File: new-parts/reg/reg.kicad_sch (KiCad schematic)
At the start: 51 parts, among them J1 BHR-10-VUA, J2 BHR-10-VUA, J3 BHR-10-VUA, J4 BHR-10-VUA, J5 Conn_01x01, J6 Conn_02x02_Odd_Even, K1 J104D2C12VDC.15S, K10 J104D2C12VDC.15S, K11 J104D2C12VDC.15S, K12 J104D2C12VDC.15S, K2 J104D2C12VDC.15S, K3 J104D2C12VDC.15S, K4 J104D2C12VDC.15S, K5 J104D2C12VDC.15S, K6 J104D2C12VDC.15S, K7 J104D2C12VDC.15S, K8 J104D2C12VDC.15S, K9 J104D2C12VDC.15S

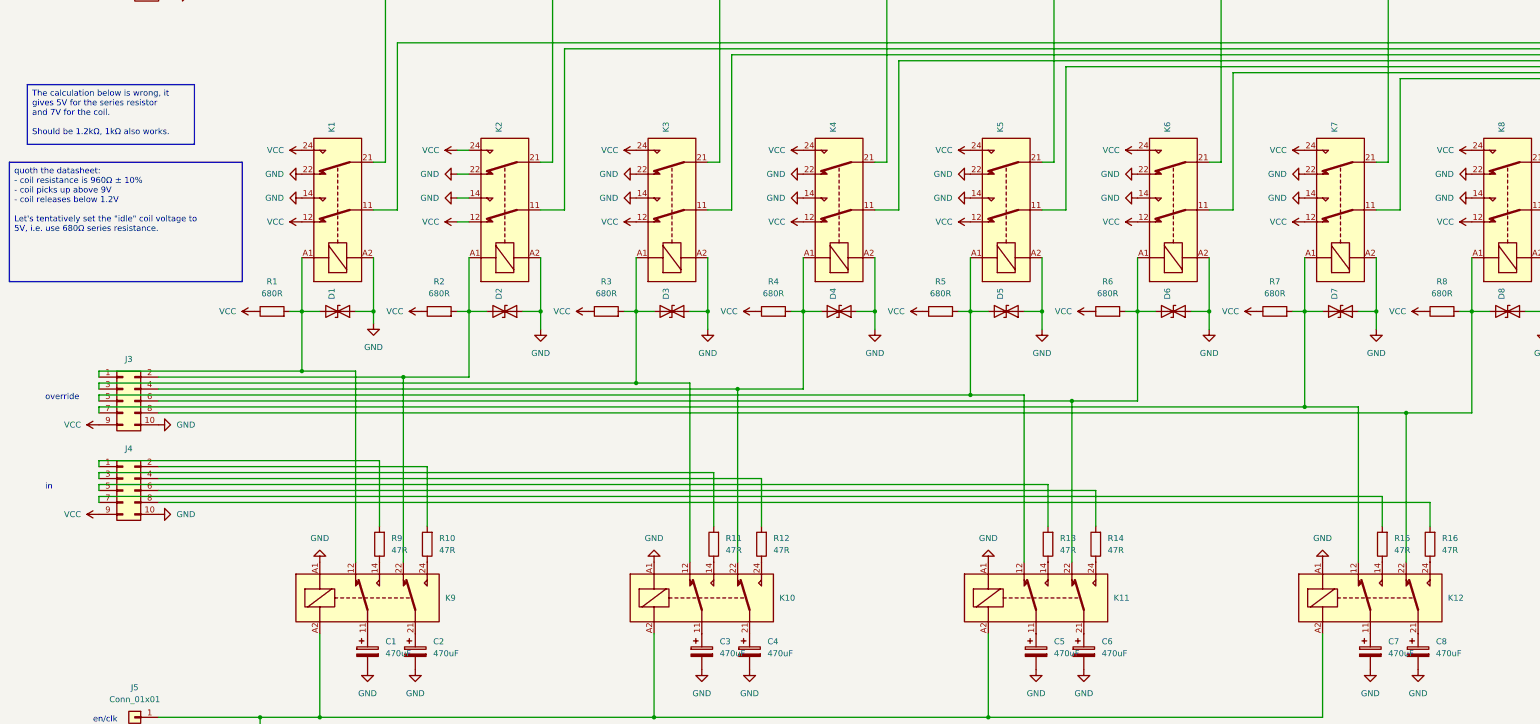
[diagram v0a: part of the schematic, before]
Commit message: reg: Correct "latching" coils' voltage dividers (finally).
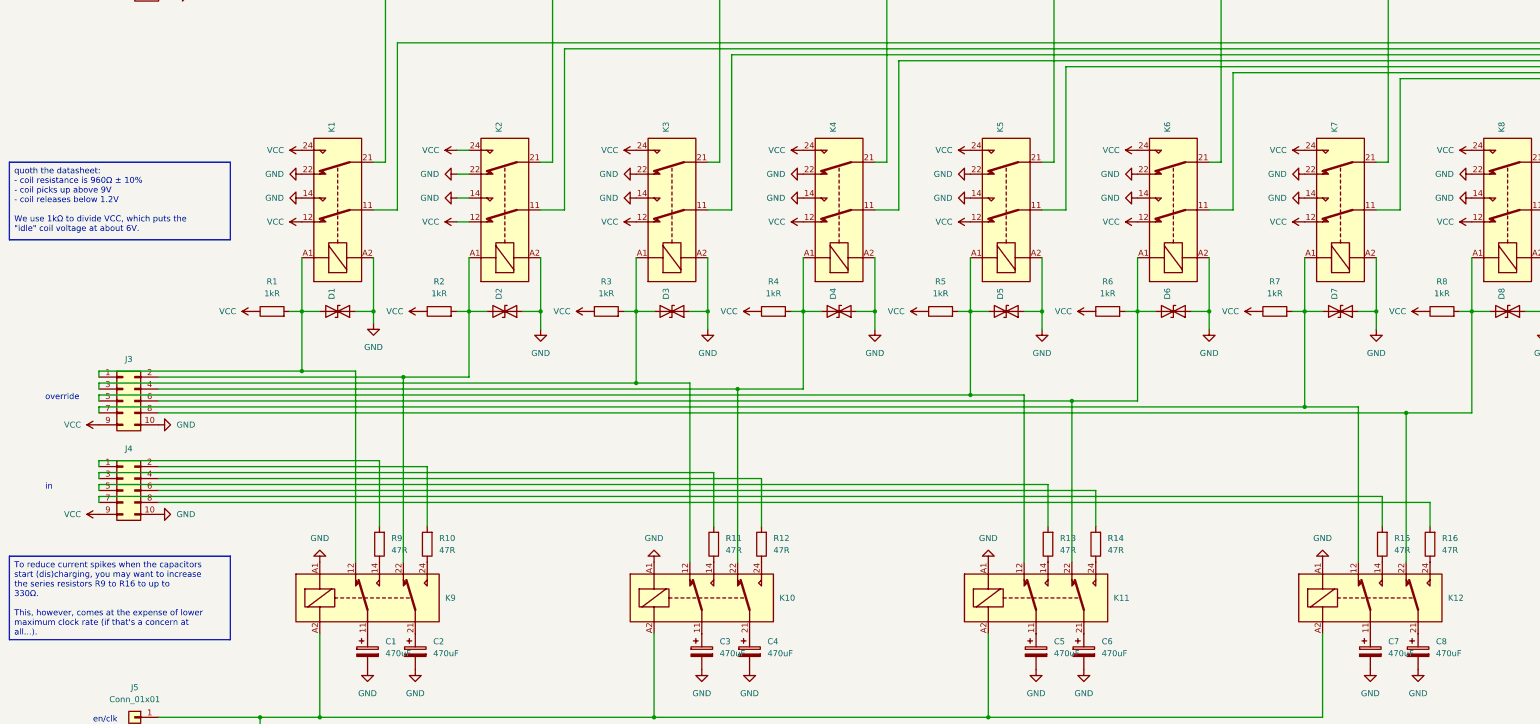
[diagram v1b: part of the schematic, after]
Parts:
- R1, R2, R3, R4, R5, R6, R7, R8: value 680R -> 1kR
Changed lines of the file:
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@@
 		)
 	)
-	(text_box "quoth the datasheet:\n- coil resistance is 960Ω ± 10%\n- coil picks up above 9V\n- coil releases below 1.2V\n\nLet's tentatively set the \"idle\" coil voltage to 5V, i.e. use 680Ω series resistance."
+	(text_box "quoth the datasheet:\n- coil resistance is 960Ω ± 10%\n- coil picks up above 9V\n- coil releases below 1.2V\n\nWe use 1kΩ to divide VCC, which puts the \"idle\" coil voltage at about 6V."
 		(exclude_from_sim no)
 		(at 16.51 74.93 0)
-		(size 49.53 25.4)
+		(size 46.99 16.51)
 		(stroke
 			(width 0)
@@
 		)
 	)
-	(text_box "The calculation below is wrong, it gives 5V for the series resistor and 7V for the coil.\n\nShould be 1.2kΩ, 1kΩ also works. "
+	(text_box "To reduce current spikes when the capacitors start (dis)charging, you may want to increase the series resistors R9 to R16 to up to 330Ω.\n\nThis, however, comes at the expense of lower maximum clock rate (if that's a concern at all...)."
 		(exclude_from_sim no)
-		(at 20.32 58.42 0)
-		(size 35.56 12.7)
+		(at 16.51 158.75 0)
+		(size 46.99 17.78)
 		(stroke
 			(width 0)
 			(type default)
-			(color 255 0 0 1)
 		)
 		(fill
@@
 			(font
 				(size 1.27 1.27)
-				(color 255 0 0 1)
 			)
 			(justify left top)
@@
 			)
 		)
-		(property "Value" "680R"
+		(property "Value" "1kR"
 			(at 107.95 102.87 90)
 			(effects
@@
 			)
 		)
-		(property "Value" "680R"
+		(property "Value" "1kR"
 			(at 214.63 102.87 90)
 			(effects
@@
 			)
 		)
-		(property "Value" "680R"
+		(property "Value" "1kR"
 			(at 143.51 102.87 90)
 			(effects
@@
 			)
 		)
-		(property "Value" "680R"
+		(property "Value" "1kR"
 			(at 250.19 102.87 90)
 			(effects
@@
 			)
 		)
-		(property "Value" "680R"
+		(property "Value" "1kR"
 			(at 72.39 102.87 90)
 			(effects
@@
 			)
 		)
-		(property "Value" "680R"
+		(property "Value" "1kR"
 			(at 179.07 102.87 90)
 			(effects
@@
 			)
 		)
-		(property "Value" "680R"
+		(property "Value" "1kR"
 			(at 321.31 102.87 90)
 			(effects
@@
 			)
 		)
-		(property "Value" "680R"
+		(property "Value" "1kR"
 			(at 285.75 102.87 90)
 			(effects
